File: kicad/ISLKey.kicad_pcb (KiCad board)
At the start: 2 copper layers, 172.5 x 109.4 mm, 44 parts, among them J1 TTGO Left, J10 5-60V AC/DC IN, J11 12V OUT (lock/aux), J13 TTGO batt pads, J14 18650 pack, J2 TTGO Right, J3 Exit btn, J4 Door contact, J5 Tamper, J6 LOCK COM/NO/NC, J7 AUX COM/NO/NC, J8 Fire volt-free, J9 Fire link COM-Fire, K1 SRD-05VDC-SL-C, K2 SRD-05VDC-SL-C, Q1 PN2222A, Q2 PN2222A, U1 PC817, U3 ISO DCDC ->12V (e.g. Mornsun 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, U4 BUCK 12->5V (e.g. MP1584)

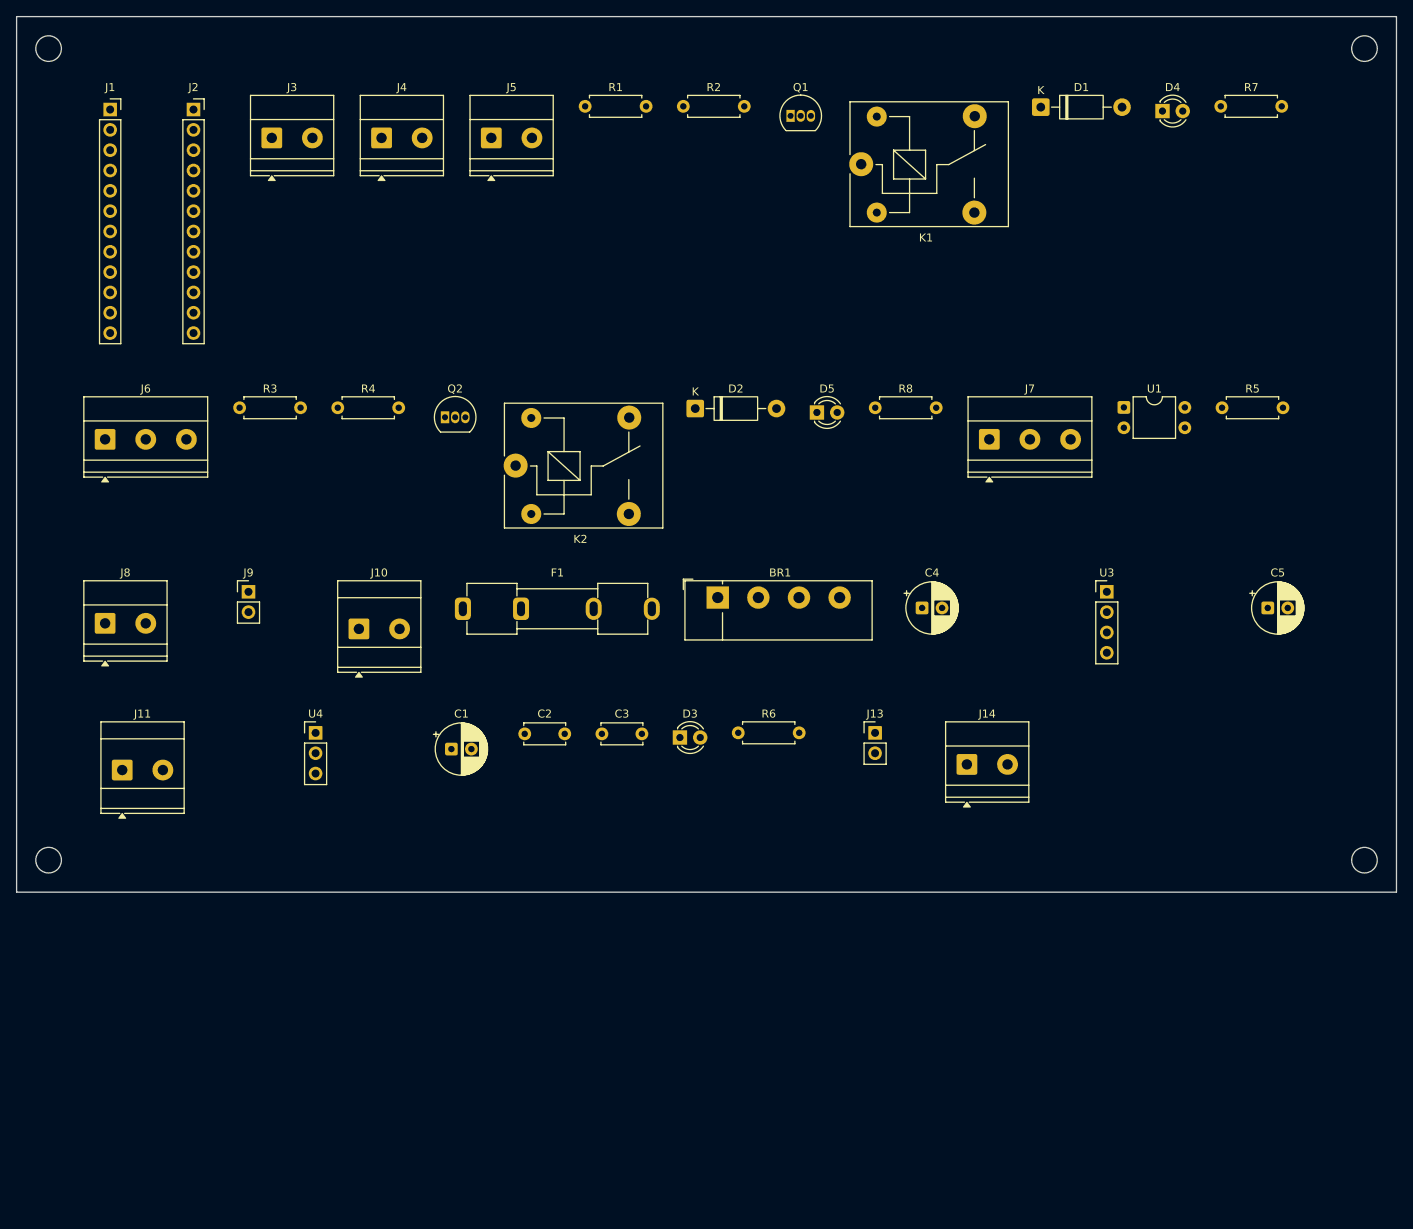
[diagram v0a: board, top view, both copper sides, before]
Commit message: kicad: use real Traco parts for the wide-input PSU
Replace the two generic module-header placeholders with genuine parts +
KiCad footprints:
- U3 isolated 12V: Traco TEN20-2412WIN (9-36V in -> isolated 12V/20W),
  footprint Converter_DCDC_TRACO_TEN20-xxxx_THT. Remote pin left open
  (positive logic, open = ON); Trim pin NC.
- U4 buck 12->5V for the TTGO: Traco TSR-1-2450 (SIP-3), footprint
  Converter_DCDC_TRACO_TSR-1_THT.
- Add PWR_FLAG on the raw primary rails (RAWP/PGND) so ERC sees them driven
  (bridge diode outputs are 'passive'); flags excluded from board + BOM.

ERC 0/0, DRC 0 (unrouted ratsnest only). One board covers 12/24V systems;
pin-compatible TEN20-4812WIN swaps in for 48V.

Co-Authored-By: Claude Opus 4.8 <noreply@anthropic.com>
Claude-Session: https://claude.ai/code/session_01WaJbCVpNNC7xF4fkqWpjpA
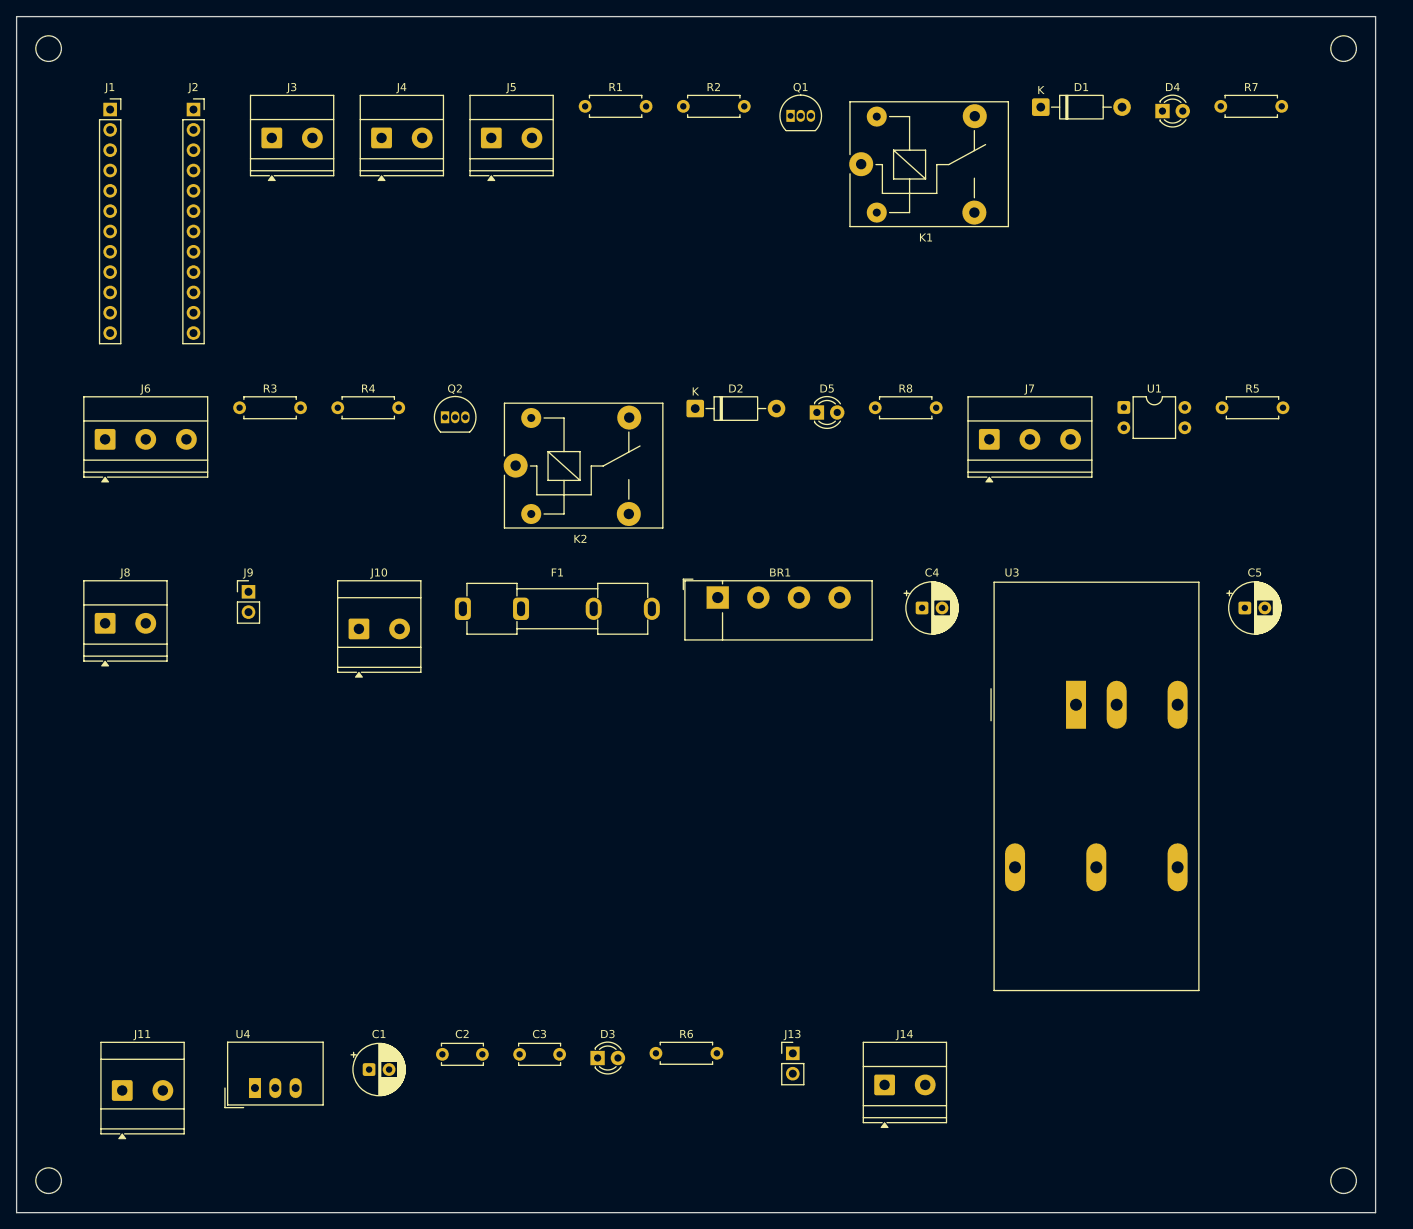
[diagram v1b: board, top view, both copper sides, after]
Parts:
- U3: value ISO DCDC ->12V (e.g. Mornsun URB) -> TEN20-2412WIN; footprint PinHeader_1x04_P2.54mm_Vertical -> Converter_DCDC_TRACO_TEN20-xxxx_THT
- U4: value BUCK 12->5V (e.g. MP1584) -> TSR-1-2450; footprint PinHeader_1x03_P2.54mm_Vertical -> Converter_DCDC_TRACO_TSR-1_THT
- moved U4 45.0 mm to (29.8, 133.9)
- moved C1 41.4 mm to (44.1, 131.6)
- moved C2 41.4 mm to (53.2, 129.7)
- moved C3 41.4 mm to (62.9, 129.7)
- moved D3 41.4 mm to (72.6, 130.2)
- moved R6 41.4 mm to (79.9, 129.6)
- moved J13 41.4 mm to (97.0, 129.6)
- moved J14 41.4 mm to (108.5, 133.5)
- moved H3 40.1 mm to (165.9, 145.5)
- moved H4 40.1 mm to (4.00, 145.5)
- moved J11 40.1 mm to (13.2, 134.2)
- moved U3 14.6 mm to (132.4, 86.0)
- moved C5 2.86 mm to (153.5, 73.9)
- moved H2 2.61 mm to (165.9, 4.00)
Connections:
- U3 pad 3: GND -> +12V
- U3 pad 4: +12V -> (no net)
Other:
- board size 172.5 x 109.4 mm -> 169.9 x 149.5 mm

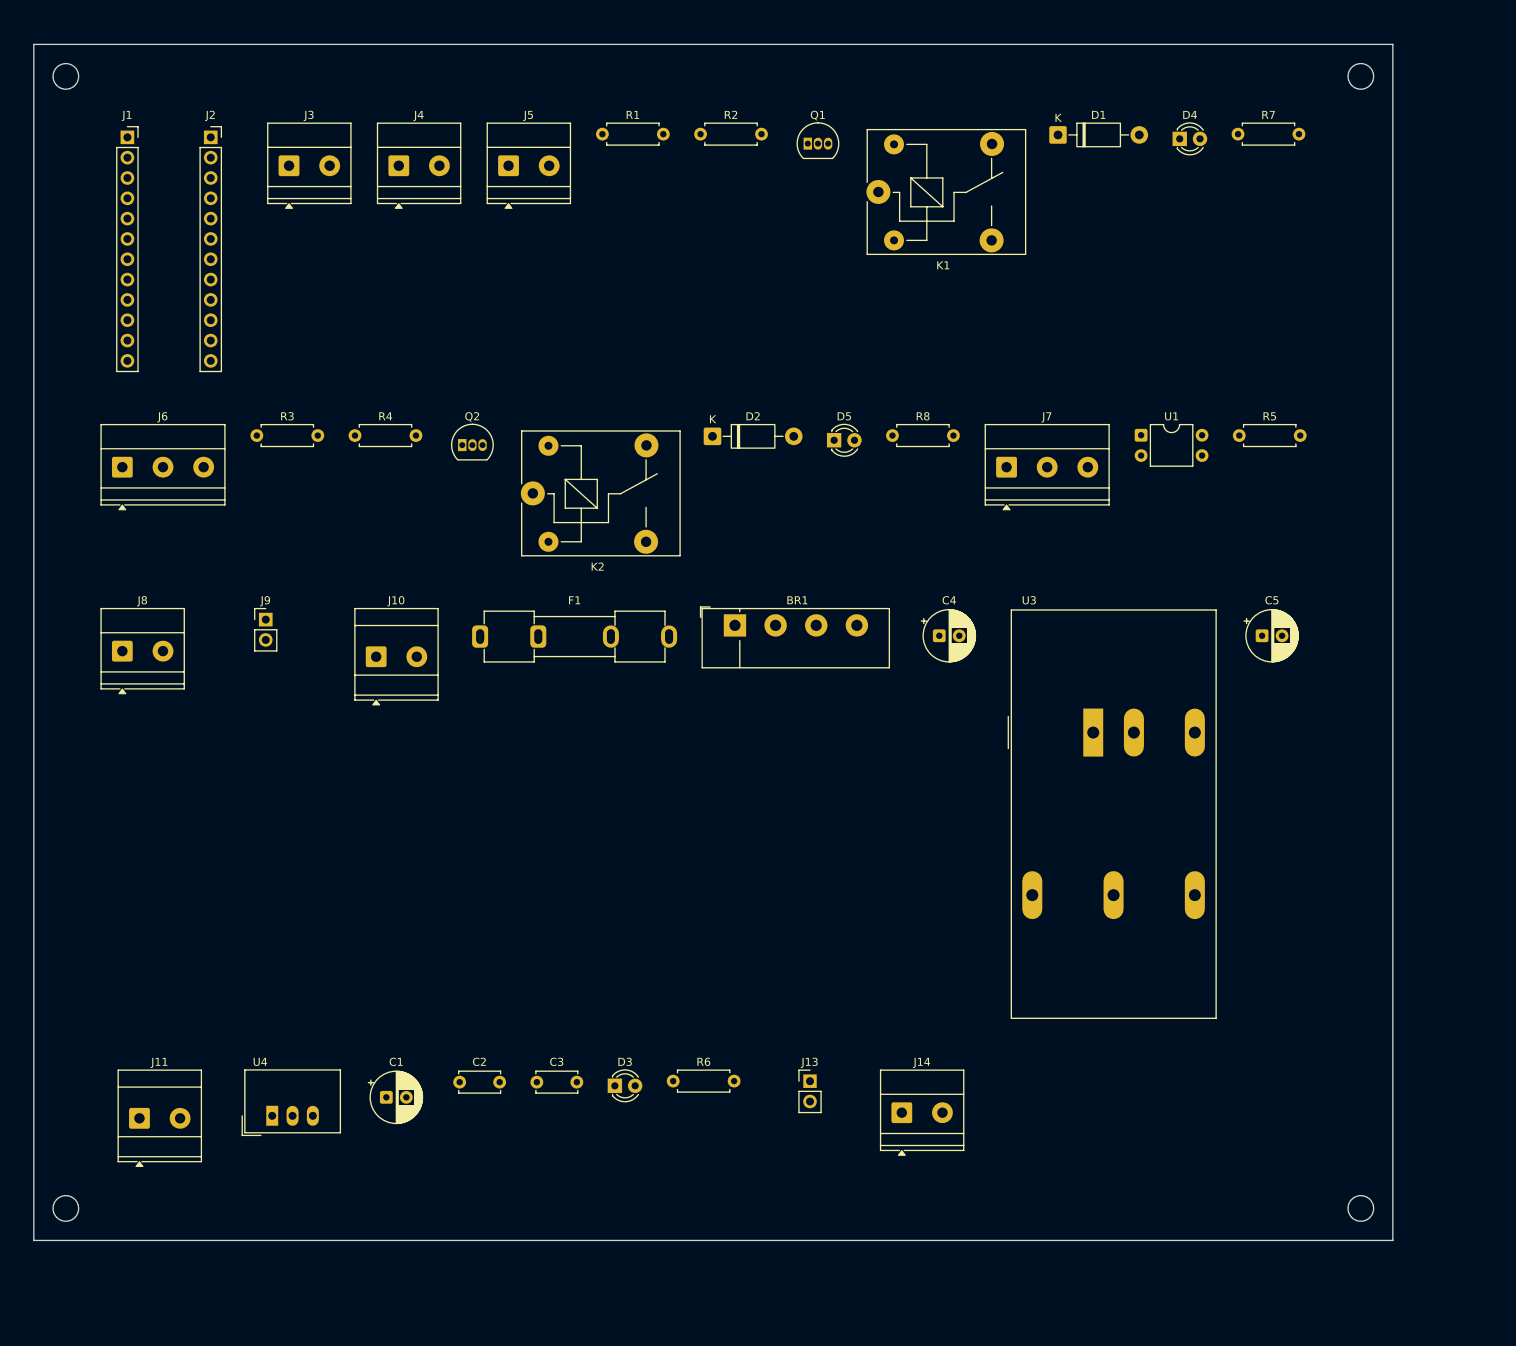
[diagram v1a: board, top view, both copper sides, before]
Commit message: kicad: real TTGO T-Display footprint + routing-aware placement
- Replace the two guessed 1x12 header sockets with a single correct TTGO
  T-Display module footprint + symbol (from GillesOdb/ttgo-tdisplay-kicad,
  legacy .kicad_mod + .lib converted to KiCad 10). Confirms the 22.86mm
  header row spacing. Pad<->GPIO verified against the module pinout
  (pad7=GPIO32, 6=GPIO33, 5=GPIO25, 4=GPIO26, 3=GPIO27, 20=GPIO13,
  1=5V, 2/13/14/22/23=GND, 12/24=3V3); symbol pins retyped passive.
- Local libs: lib/ISLKey.pretty + lib/ISLKey.kicad_sym, with project
  fp-lib-table / sym-lib-table so KiCad resolves them.
- make_pcb.py: routing-aware floorplan (inputs on left edge, TTGO centre,
  each relay driver->coil->contacts->terminal in line, fire monitor row,
  power chain along the bottom with the U3 isolation barrier splitting
  primary/secondary). Power row auto-spaced by real footprint width.

ERC 0/0. DRC: no physical collisions (only cosmetic silk/text-height from
the imported footprint's 0.75mm silk). Board ~185x164mm, ratsnest ready.

Co-Authored-By: Claude Opus 4.8 <noreply@anthropic.com>
Claude-Session: https://claude.ai/code/session_01WaJbCVpNNC7xF4fkqWpjpA
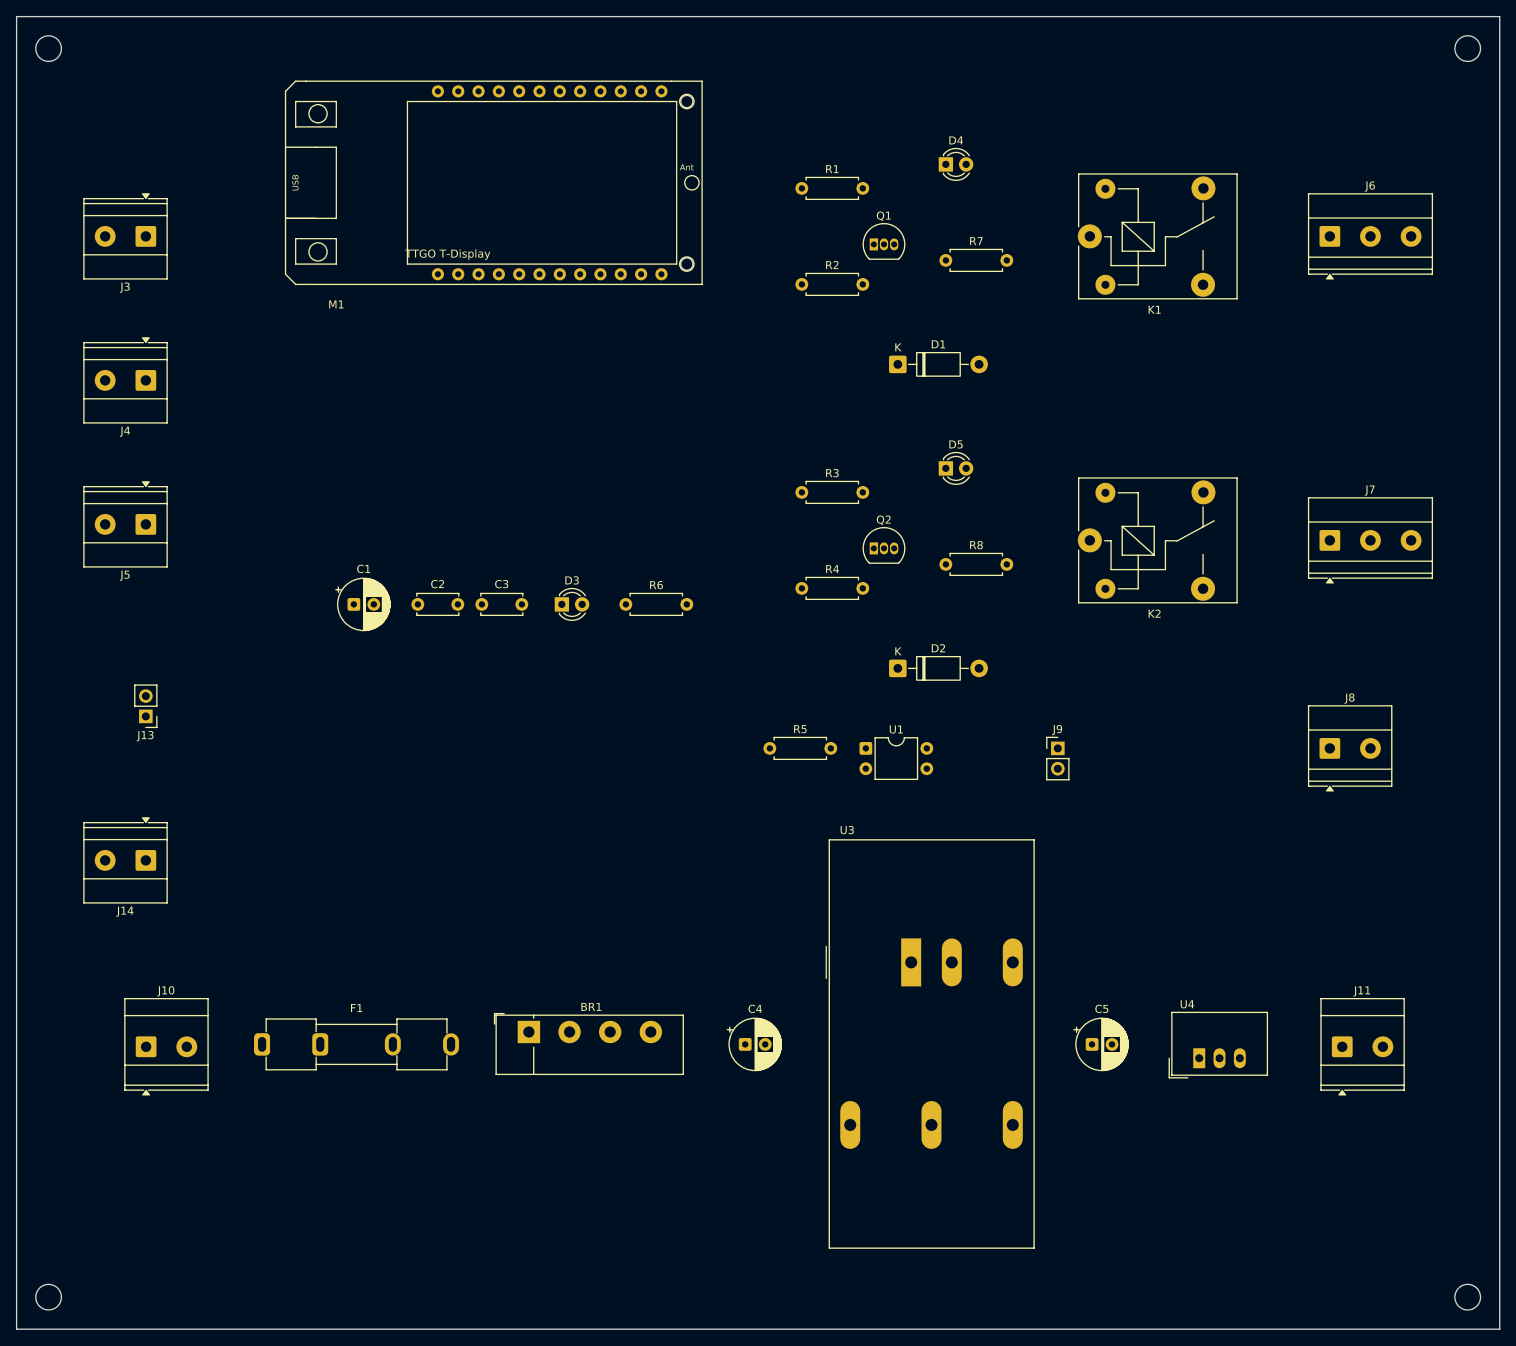
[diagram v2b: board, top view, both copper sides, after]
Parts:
- removed J1: TTGO Left, PinSocket_1x12_P2.54mm_Vertical
- removed J2: TTGO Right, PinSocket_1x12_P2.54mm_Vertical
- added M1: TTGO T-Display, TTGO_ESP32_TDisplay_v1.1, F.Cu at (34.0, 30.0)
- moved J6 153.7 mm to (162.0, 24.0)
- moved J8 151.4 mm to (162.0, 88.0)
- moved J11 150.6 mm to (163.6, 125.3)
- moved U4 116.1 mm to (145.7, 126.7)
- moved J9 100.3 mm to (128.0, 88.0)
- moved J14 99.6 mm to (14.0, 102.0), turned to 180 degrees
- moved J13 94.7 mm to (14.0, 84.0), turned to 180 degrees
- moved R5 70.5 mm to (92.0, 88.0)
- moved K2 69.9 mm to (132.0, 62.0)
- moved R3 68.5 mm to (96.0, 56.0)
- moved J5 63.8 mm to (14.0, 60.0), turned to 180 degrees
- moved C1 61.8 mm to (40.0, 70.0)
- moved D3 60.5 mm to (66.0, 70.0)
- moved C3 60.1 mm to (56.0, 70.0)
- moved C2 59.9 mm to (48.0, 70.0)
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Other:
- board size 169.9 x 149.5 mm -> 185.4 x 164.1 mm
